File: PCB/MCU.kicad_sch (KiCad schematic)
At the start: 0 parts

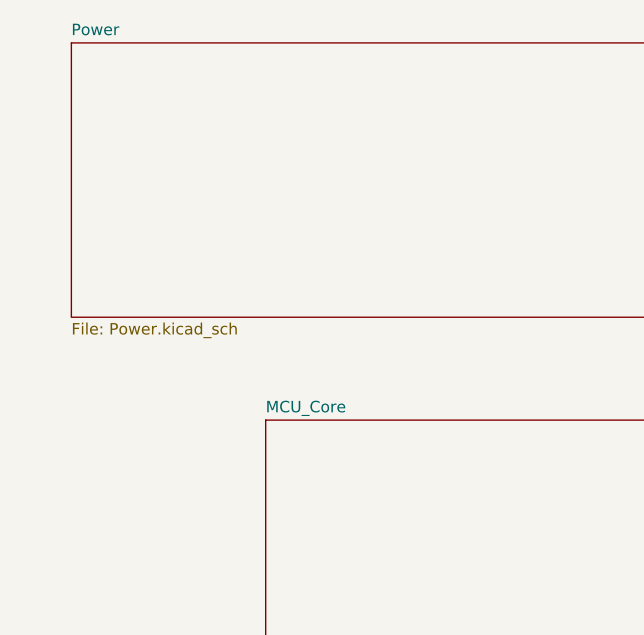
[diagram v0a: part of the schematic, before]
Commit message: ADD supplies to UC
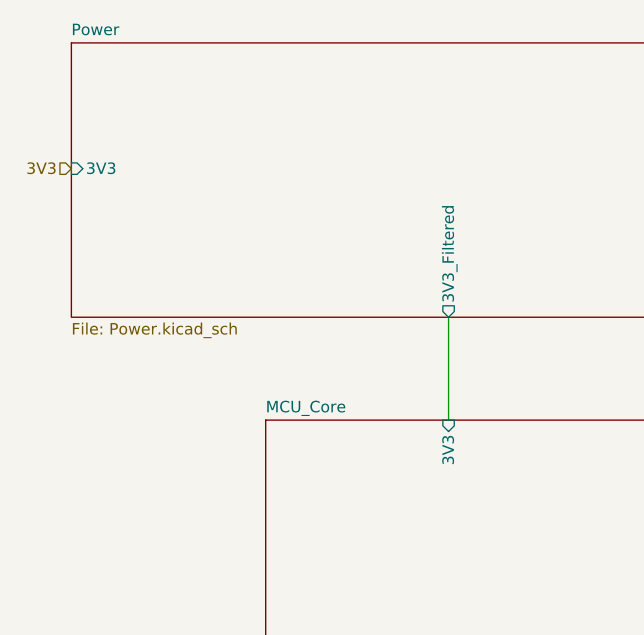
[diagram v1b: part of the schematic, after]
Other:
- sheet MCU_Core ports: added 3V3; removed none
- sheet Power ports: added 3V3, 3V3_Filtered; removed none
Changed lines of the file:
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@@
 	(generator_version "9.0")
 	(paper "A4")
+	(wire
+		(pts
+			(xy 68.58 53.34) (xy 68.58 64.77)
+		)
+		(stroke
+			(width 0)
+			(type default)
+		)
+	)
+	(hierarchical_label "3V3"
+		(shape input)
+		(at 26.67 36.83 180)
+		(effects
+			(font
+				(size 1.27 1.27)
+			)
+			(justify right)
+		)
+	)
 	(sheet
 		(at 194.31 77.47)
@@
 			)
 		)
+		(pin "3V3" input
+			(at 26.67 36.83 180)
+			(effects
+				(font
+					(size 1.27 1.27)
+				)
+				(justify left)
+			)
+		)
+		(pin "3V3_Filtered" output
+			(at 68.58 53.34 270)
+			(effects
+				(font
+					(size 1.27 1.27)
+				)
+				(justify left)
+			)
+		)
 		(instances
 			(project "PCB"
@@
 			(effects
 				(font
+					(size 1.27 1.27)
+				)
+				(justify right)
+			)
+		)
+		(pin "3V3" input
+			(at 68.58 64.77 90)
+			(effects
+				(font

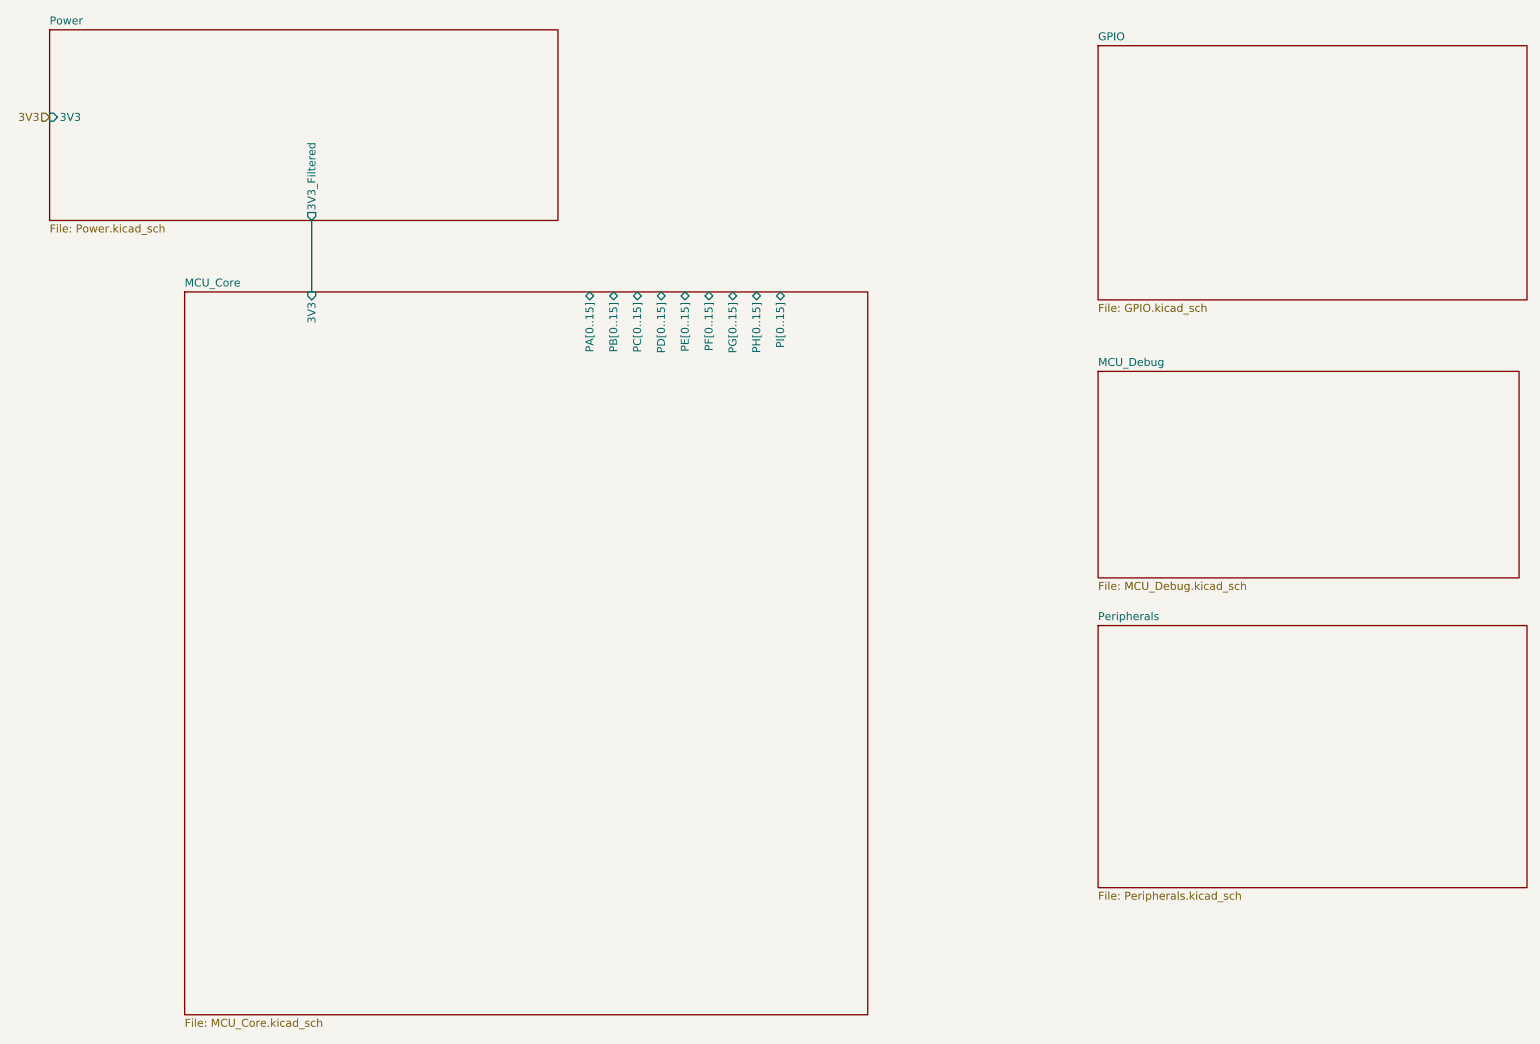
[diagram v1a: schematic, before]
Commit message: Updated MCU sheet
Added decoupling capacitors
Linked Ethernet to MCU
Started Usb linking to MCU
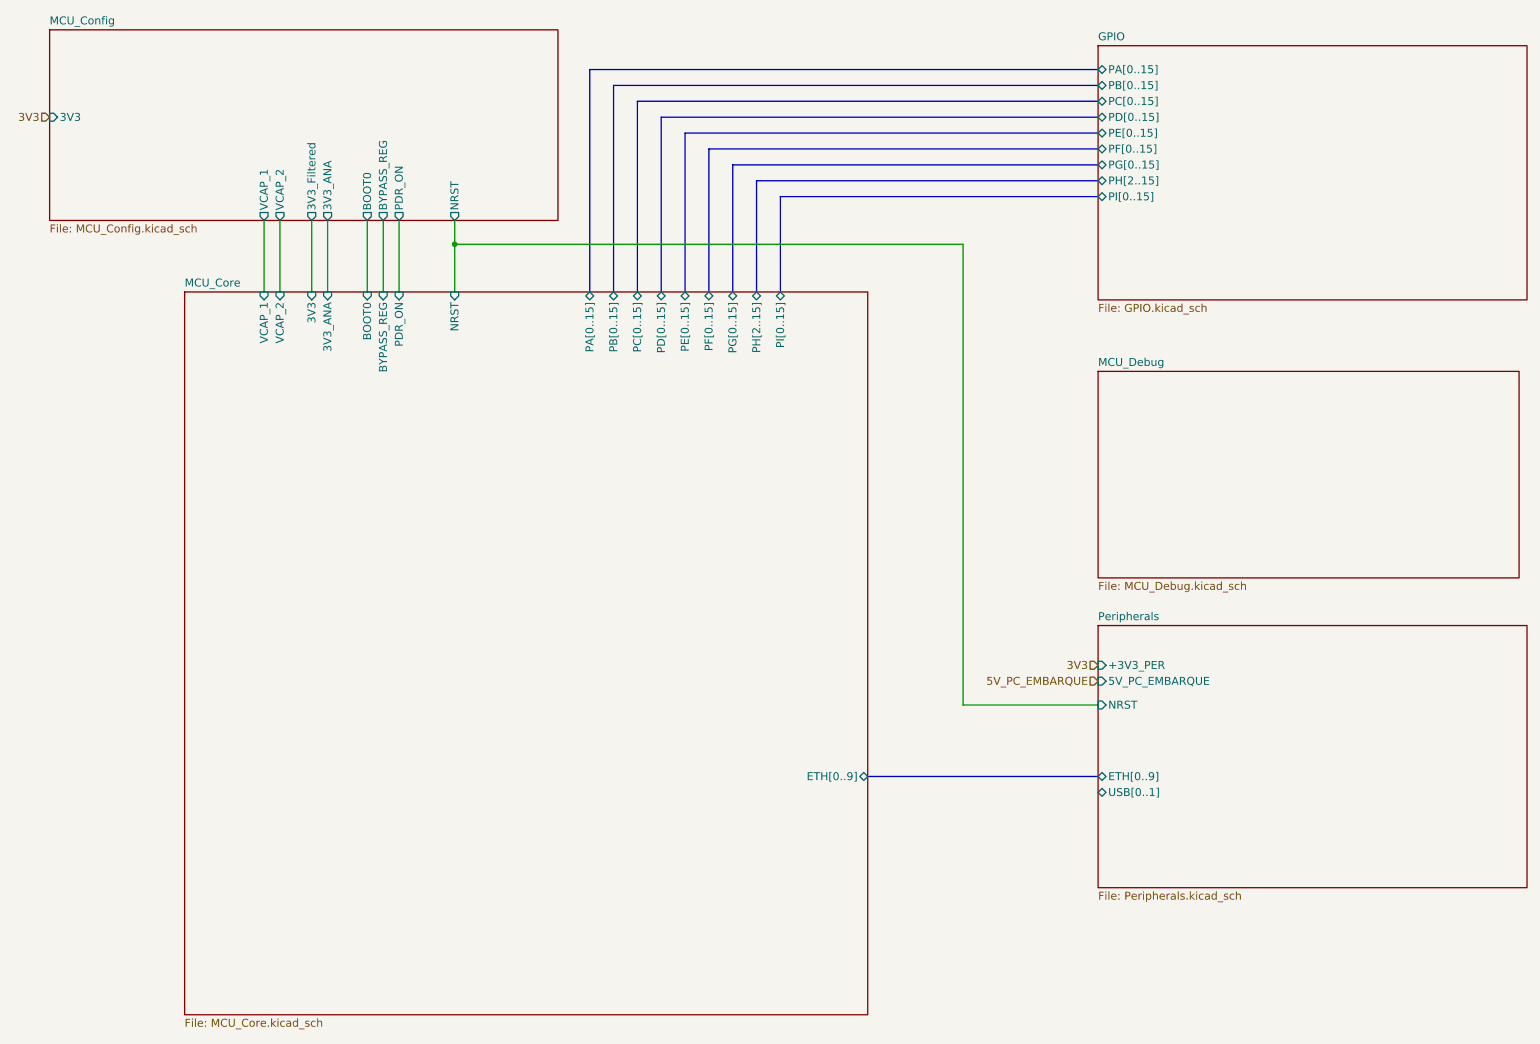
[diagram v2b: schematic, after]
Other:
- sheet Power renamed MCU_Config
- sheet GPIO ports: added PA[0..15], PB[0..15], PC[0..15], PD[0..15], PE[0..15], PF[0..15], PG[0..15], PH[2..15], PI[0..15]; removed none
- sheet MCU_Config: file Power.kicad_sch -> MCU_Config.kicad_sch
- sheet MCU_Config ports: added 3V3_ANA, BOOT0, BYPASS_REG, NRST, PDR_ON, VCAP_1, VCAP_2; removed none
- sheet MCU_Core ports: added 3V3_ANA, BOOT0, BYPASS_REG, ETH[0..9], NRST, PDR_ON, PH[2..15], VCAP_1, VCAP_2; removed PH[0..15]
- sheet Peripherals ports: added +3V3_PER, 5V_PC_EMBARQUE, ETH[0..9], NRST, USB[0..1]; removed none

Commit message: Updated a lot of stuff:
Added encoders,
Added 5V power supply for actuators
Added 12V power supply for actuators
Renamed sheets to be clearer
Added usb debug
Modify MCU sheet to be A3 format
Linked some pins
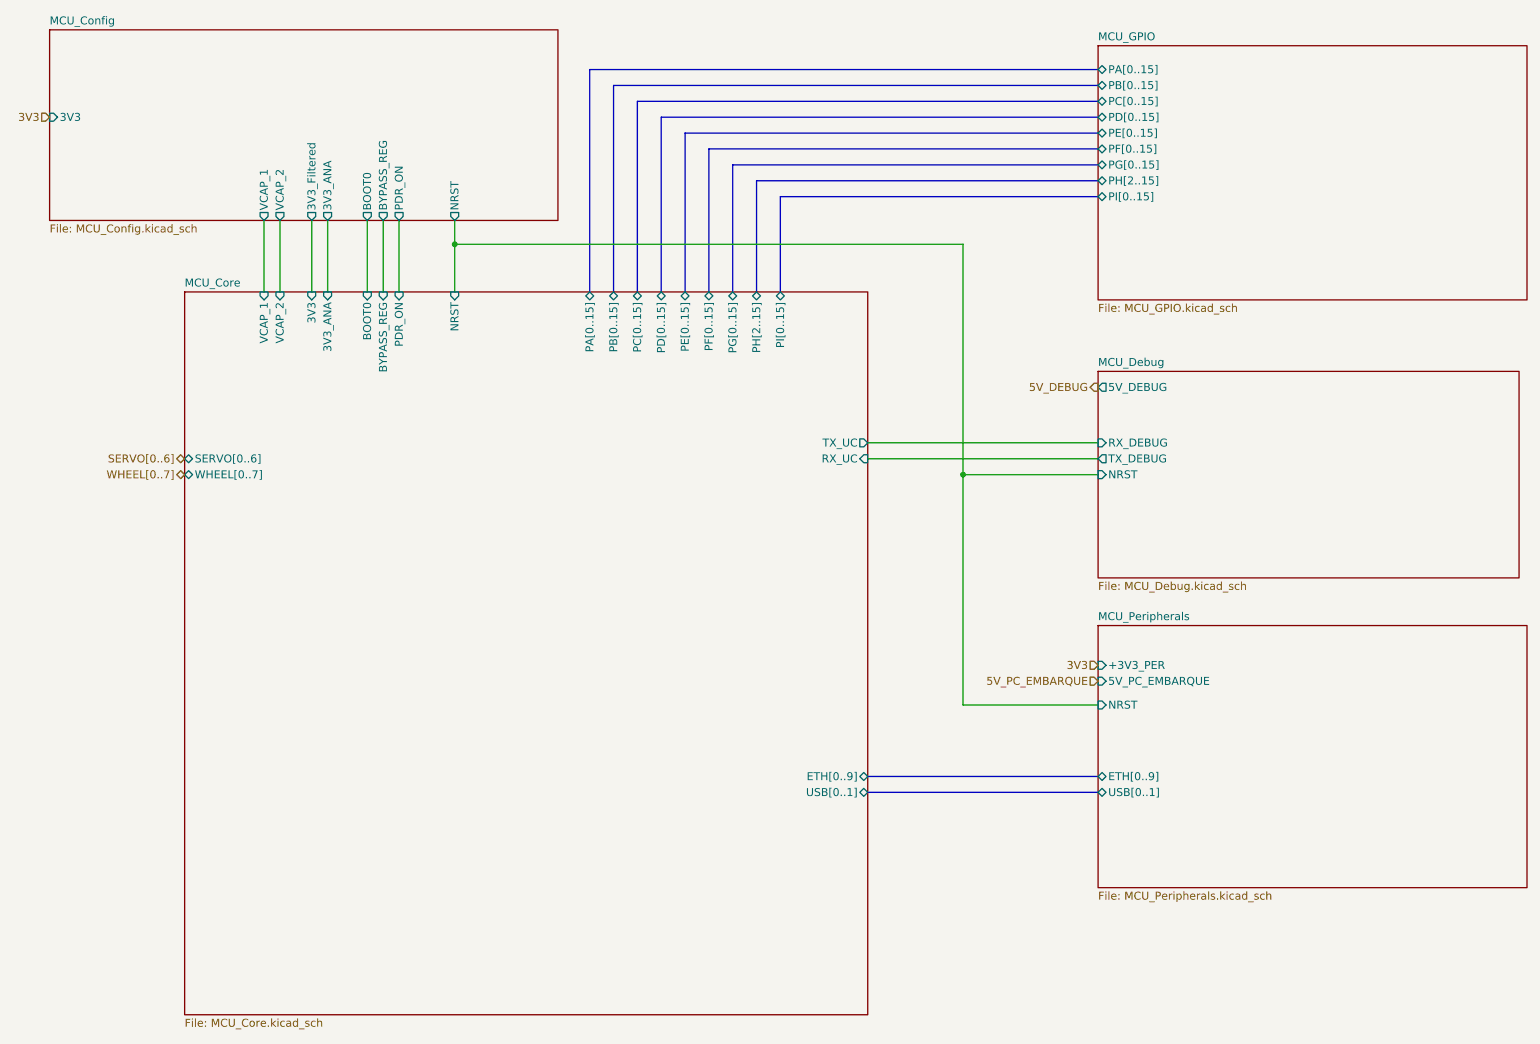
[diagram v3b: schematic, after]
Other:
- sheet GPIO renamed MCU_GPIO
- sheet Peripherals renamed MCU_Peripherals
- sheet MCU_Core ports: added RX_UC, SERVO[0..6], TX_UC, USB[0..1], WHEEL[0..7]; removed none
- sheet MCU_Debug ports: added 5V_DEBUG, NRST, RX_DEBUG, TX_DEBUG; removed none
- sheet MCU_GPIO: file GPIO.kicad_sch -> MCU_GPIO.kicad_sch
- sheet MCU_Peripherals: file Peripherals.kicad_sch -> MCU_Peripherals.kicad_sch
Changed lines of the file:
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@@
 	(paper "A4")
+	(junction
+		(at 172.72 93.98)
+		(diameter 0)
+		(color 0 0 0 0)
+	)
 	(junction
 		(at 91.44 57.15)
@@
 	(bus
 		(pts
+			(xy 157.48 144.78) (xy 194.31 144.78)
+		)
+		(stroke
+			(width 0)
+			(type default)
+		)
+	)
+	(wire
+		(pts
+			(xy 172.72 93.98) (xy 194.31 93.98)
+		)
+		(stroke
+			(width 0)
+			(type default)
+		)
+	)
+	(wire
+		(pts
+			(xy 157.48 91.44) (xy 194.31 91.44)
+		)
+		(stroke
+			(width 0)
+			(type default)
+		)
+	)
+	(bus
+		(pts
 			(xy 194.31 29.21) (xy 113.03 29.21)
 		)
@@
 		)
 	)
+	(wire
+		(pts
+			(xy 157.48 88.9) (xy 194.31 88.9)
+		)
+		(stroke
+			(width 0)
+			(type default)
+		)
+	)
 	(bus
 		(pts
@@
 	(wire
 		(pts
+			(xy 172.72 93.98) (xy 172.72 130.81)
+		)
+		(stroke
+			(width 0)
+			(type default)
+		)
+	)
+	(wire
+		(pts
 			(xy 82.55 53.34) (xy 82.55 64.77)
 		)
@@
 	(wire
 		(pts
-			(xy 172.72 57.15) (xy 172.72 130.81)
+			(xy 172.72 57.15) (xy 172.72 93.98)
 		)
 		(stroke
@@
 			(width 0)
 			(type default)
+		)
+	)
+	(hierarchical_label "WHEEL[0..7]"
+		(shape bidirectional)
+		(at 48.26 93.98 180)
+		(effects
+			(font
+				(size 1.27 1.27)
+			)
+			(justify right)
 		)
 	)
@@
 		(shape input)
 		(at 26.67 36.83 180)
+		(effects
+			(font
+				(size 1.27 1.27)
+			)
+			(justify right)
+		)
+	)
+	(hierarchical_label "SERVO[0..6]"
+		(shape bidirectional)
+		(at 48.26 91.44 180)
+		(effects
+			(font
+				(size 1.27 1.27)
+			)
+			(justify right)
+		)
+	)
+	(hierarchical_label "5V_DEBUG"
+		(shape output)
+		(at 194.31 80.01 180)
 		(effects
 			(font
@@
 			)
 		)
+		(pin "5V_DEBUG" output
+			(at 194.31 80.01 180)
+			(effects
+				(font
+					(size 1.27 1.27)
+				)
+				(justify left)
+			)
+		)
+		(pin "TX_DEBUG" output
+			(at 194.31 91.44 180)
+			(effects
+				(font
+					(size 1.27 1.27)
+				)
+				(justify left)
+			)
+		)
+		(pin "RX_DEBUG" input
+			(at 194.31 88.9 180)
+			(effects
+				(font
+					(size 1.27 1.27)
+				)
+				(justify left)
+			)
+		)
+		(pin "NRST" input
+			(at 194.31 93.98 180)
+			(effects
+				(font
+					(size 1.27 1.27)
+				)
+				(justify left)
+			)
+		)
 		(instances
 			(project "PCB"
@@
 			(color 0 0 0 0.0000)
 		)
-		(property "Sheetname" "Peripherals"
+		(property "Sheetname" "MCU_Peripherals"
 			(at 194.31 117.3984 0)
 			(effects
@@
 			)
 		)
-		(property "Sheetfile" "Peripherals.kicad_sch"
+		(property "Sheetfile" "MCU_Peripherals.kicad_sch"
 			(at 194.31 160.6046 0)
 			(effects
@@
 			)
 		)
+		(pin "USB[0..1]" bidirectional
+			(at 157.48 144.78 0)
+			(effects
+				(font
+					(size 1.27 1.27)
+				)
+				(justify right)
+			)
+		)
+		(pin "RX_UC" input
+			(at 157.48 91.44 0)
+			(effects
+				(font
+					(size 1.27 1.27)
+				)
+				(justify right)
+			)
+		)
+		(pin "TX_UC" output
+			(at 157.48 88.9 0)
+			(effects
+				(font
+					(size 1.27 1.27)
+				)
+				(justify right)
+			)
+		)
+		(pin "SERVO[0..6]" bidirectional
+			(at 48.26 91.44 180)
+			(effects
+				(font
+					(size 1.27 1.27)
+				)
+				(justify left)
+			)
+		)
+		(pin "WHEEL[0..7]" bidirectional
+			(at 48.26 93.98 180)
+			(effects
+				(font
+					(size 1.27 1.27)
+				)
+				(justify left)
+			)
+		)
 		(instances
 			(project "PCB"
@@
 			(color 0 0 0 0.0000)
 		)
-		(property "Sheetname" "GPIO"
+		(property "Sheetname" "MCU_GPIO"
 			(at 194.31 24.6884 0)
 			(effects
@@
 			)
 		)
-		(property "Sheetfile" "GPIO.kicad_sch"
+		(property "Sheetfile" "MCU_GPIO.kicad_sch"
 			(at 194.31 66.6246 0)
 			(effects
